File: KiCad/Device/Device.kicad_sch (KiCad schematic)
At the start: 29 parts, among them IC1 ATTINY167-XUR, J1 Mikrofon, J2 Lysføler, J3 Optisk sensor, J4 Fugtføler, J5 VCC, J6 ESP8266(wifi), J7 Conn_02x06_Counter_Clockwise, SW1 SW_MEC_5E, SW3 SW_MEC_5E, SW4 SW_DIP_x02, Y1 Crystal

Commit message: save
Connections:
- net +5V: now also J7.11 (Pin_11); no longer J7.12 (Pin_12)
- net UPWR: now also J7.12 (Pin_12); no longer J7.11 (Pin_11)
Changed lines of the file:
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@@
     (stroke (width 0) (type default) (color 0 0 0 0))
   )
-  (wire (pts (xy 243.84 119.38) (xy 229.87 119.38))
+  (wire (pts (xy 243.84 119.38) (xy 234.95 119.38))
     (stroke (width 0) (type default) (color 0 0 0 0))
   )
@@
     (stroke (width 0) (type default) (color 0 0 0 0))
   )
+  (wire (pts (xy 256.54 119.38) (xy 267.335 119.38))
+    (stroke (width 0) (type default) (color 0 0 0 0))
+  )
   (wire (pts (xy 77.47 177.8) (xy 81.28 177.8))
     (stroke (width 0) (type default) (color 0 0 0 0))
@@
     (stroke (width 0) (type default) (color 0 0 0 0))
   )
-  (wire (pts (xy 243.84 116.84) (xy 224.155 116.84))
+  (wire (pts (xy 243.84 116.84) (xy 229.235 116.84))
     (stroke (width 0) (type default) (color 0 0 0 0))
   )
@@
     )
   )
-  (global_label "UPWR" (shape input) (at 256.54 119.38 0) (fields_autoplaced)
-    (effects (font (size 1.27 1.27)) (justify left))
-    (property "Intersheet References" "${INTERSHEET_REFS}" (id 0) (at 264.275 119.4594 0)
+  (global_label "UPWR" (shape input) (at 256.54 116.84 0) (fields_autoplaced)
+    (effects (font (size 1.27 1.27)) (justify left))
+    (property "Intersheet References" "${INTERSHEET_REFS}" (id 0) (at 264.275 116.9194 0)
       (effects (font (size 1.27 1.27)) (justify left) hide)
     )
@@
     (pin "1")
   )
-  (symbol (lib_id "power:GND") (at 229.87 119.38 0) (mirror y) (unit 1)
-    (in_bom yes) (on_board yes)
-    (property "Reference" "#PWR0118" (id 0) (at 229.87 125.73 0)
-      (effects (font (size 1.27 1.27)) hide)
-    )
-    (property "Value" "GND" (id 1) (at 231.775 123.19 0)
-      (effects (font (size 1.27 1.27)) (justify left))
-    )
-    (property "Footprint" "" (id 2) (at 229.87 119.38 0)
-      (effects (font (size 1.27 1.27)) hide)
-    )
-    (property "Datasheet" "" (id 3) (at 229.87 119.38 0)
+  (symbol (lib_id "power:GND") (at 234.95 119.38 0) (mirror y) (unit 1)
+    (in_bom yes) (on_board yes)
+    (property "Reference" "#PWR0118" (id 0) (at 234.95 125.73 0)
+      (effects (font (size 1.27 1.27)) hide)
+    )
+    (property "Value" "GND" (id 1) (at 236.855 123.19 0)
+      (effects (font (size 1.27 1.27)) (justify left))
+    )
+    (property "Footprint" "" (id 2) (at 234.95 119.38 0)
+      (effects (font (size 1.27 1.27)) hide)
+    )
+    (property "Datasheet" "" (id 3) (at 234.95 119.38 0)
       (effects (font (size 1.27 1.27)) hide)
     )
@@
     (pin "2")
   )
-  (symbol (lib_id "power:+5V") (at 256.54 116.84 0) (mirror y) (unit 1)
-    (in_bom yes) (on_board yes)
-    (property "Reference" "#PWR0102" (id 0) (at 256.54 120.65 0)
-      (effects (font (size 1.27 1.27)) hide)
-    )
-    (property "Value" "+5V" (id 1) (at 259.715 115.57 0))
-    (property "Footprint" "" (id 2) (at 256.54 116.84 0)
-      (effects (font (size 1.27 1.27)) hide)
-    )
-    (property "Datasheet" "" (id 3) (at 256.54 116.84 0)
+  (symbol (lib_id "power:+5V") (at 267.335 119.38 0) (mirror y) (unit 1)
+    (in_bom yes) (on_board yes)
+    (property "Reference" "#PWR0102" (id 0) (at 267.335 123.19 0)
+      (effects (font (size 1.27 1.27)) hide)
+    )
+    (property "Value" "+5V" (id 1) (at 270.51 118.11 0))
+    (property "Footprint" "" (id 2) (at 267.335 119.38 0)
+      (effects (font (size 1.27 1.27)) hide)
+    )
+    (property "Datasheet" "" (id 3) (at 267.335 119.38 0)
       (effects (font (size 1.27 1.27)) hide)
     )
@@
     (pin "1")
   )
-  (symbol (lib_id "power:GND") (at 224.155 116.84 0) (mirror y) (unit 1)
-    (in_bom yes) (on_board yes)
-    (property "Reference" "#PWR0101" (id 0) (at 224.155 123.19 0)
-      (effects (font (size 1.27 1.27)) hide)
-    )
-    (property "Value" "GND" (id 1) (at 226.06 120.65 0)
-      (effects (font (size 1.27 1.27)) (justify left))
-    )
-    (property "Footprint" "" (id 2) (at 224.155 116.84 0)
-      (effects (font (size 1.27 1.27)) hide)
-    )
-    (property "Datasheet" "" (id 3) (at 224.155 116.84 0)
-      (effects (font (size 1.27 1.27)) hide)
-    )
+  (symbol (lib_id "power:GND") (at 229.235 116.84 0) (mirror y) (unit 1)
+    (in_bom yes) (on_board yes)
+    (property "Reference" "#PWR0101" (id 0) (at 229.235 123.19 0)
+      (effects (font (size 1.27 1.27)) hide)
+    )
+    (property "Value" "GND" (id 1) (at 231.14 120.65 0)
+      (effects (font (size 1.27 1.27)) (justify left))
+    )
+    (property "Footprint" "" (id 2) (at 229.235 116.84 0)
+      (effects (font (size 1.27 1.27)) hide)
+    )
+    (property "Datasheet" "" (id 3) (at 229.235 116.84 0)
+      (effects (font (size 1.27 1.27)) hide)
+    )

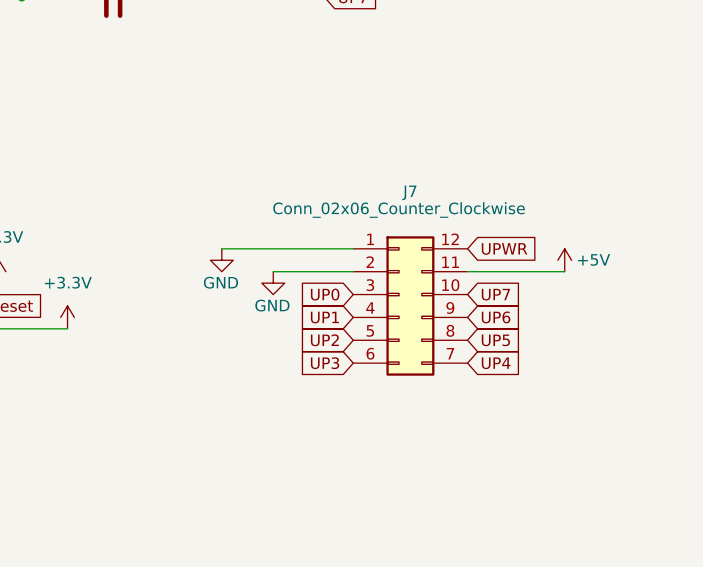
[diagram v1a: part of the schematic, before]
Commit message: Ny_connecter
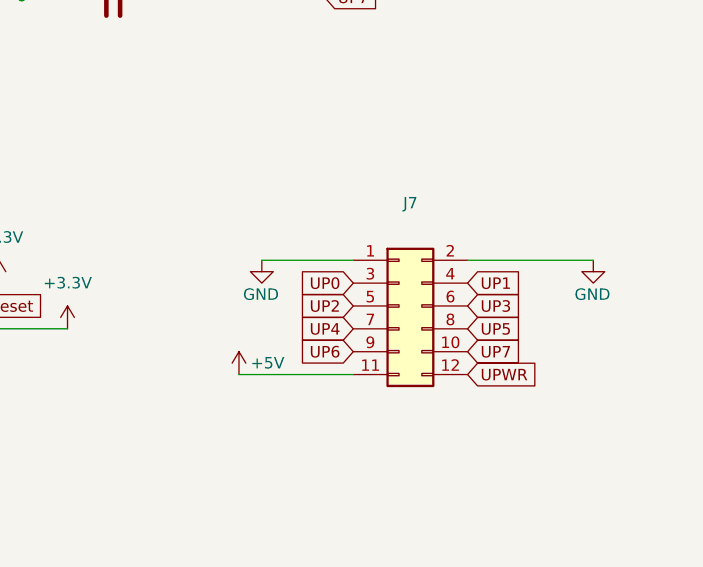
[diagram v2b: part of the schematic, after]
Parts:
- removed J7: Conn_02x06_Counter_Clockwise, Connector_PinHeader_2.54mm:PinHeader_2x06_P2.54mm_Horizontal, symbol Connector_Generic:Conn_02x06_Counter_Clockwise
- added J7: (no value), symbol Connector_Generic:Conn_02x06_Odd_Even
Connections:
- net +5V: now also J7.11 (Pin_11)
- net DHT11: now also J7.3 (Pin_3)
- net GND: now also J7.1 (Pin_1), J7.2 (Pin_2)
- net OPTISK: now also J7.6 (Pin_6)
- net PHOTRAN: now also J7.9 (Pin_9)
- net UP1: now also J7.4 (Pin_4)
- net UP2: now also J7.5 (Pin_5)
- net UP4: now also J7.7 (Pin_7)
- net UP5: now also J7.8 (Pin_8)
- net UP7: now also J7.10 (Pin_10)
- net UPWR: now also J7.12 (Pin_12)

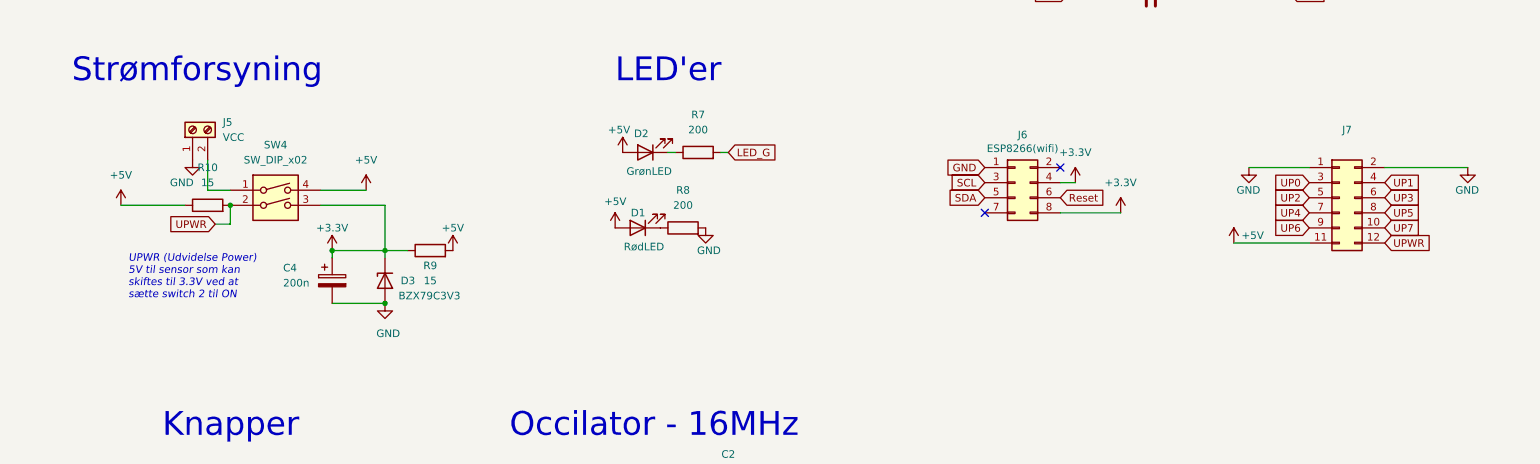
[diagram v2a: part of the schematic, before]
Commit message: Opdatering af device kicad
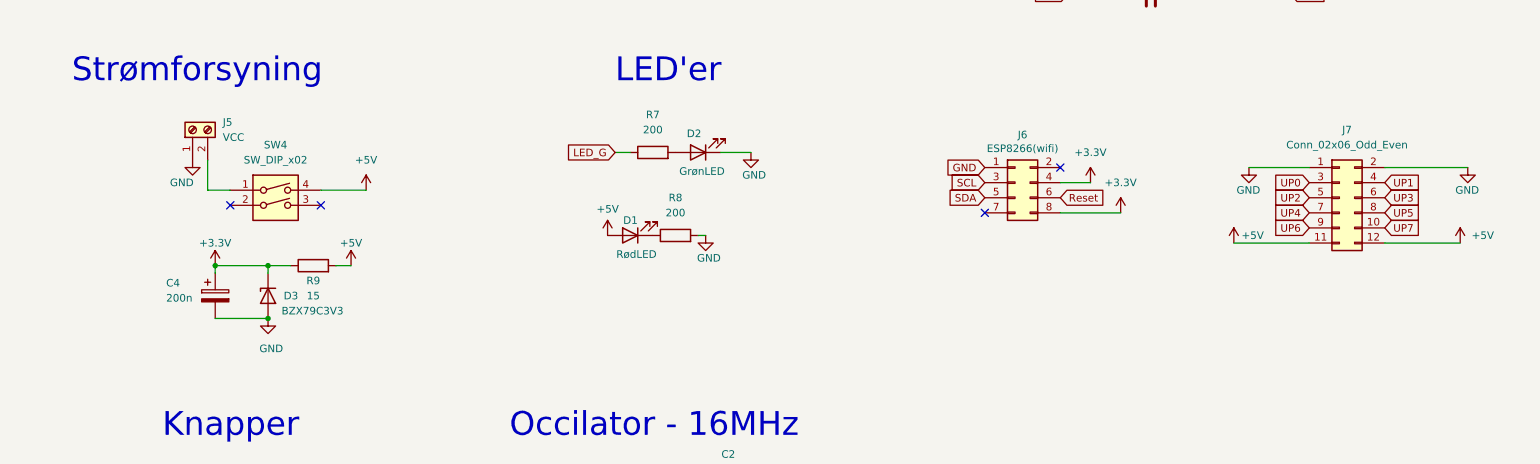
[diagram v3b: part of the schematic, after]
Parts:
- removed R10: 15, Resistor_THT:R_Axial_DIN0309_L9.0mm_D3.2mm_P12.70mm_Horizontal, symbol Device:R
- J7: value (none) -> Conn_02x06_Odd_Even; footprint (none) -> Connector_PinHeader_2.54mm:PinHeader_2x06_P2.54mm_Vertical
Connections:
- net +3V3: no longer SW4.3
- net +5V: now also J7.12 (Pin_12); no longer D2.2 (A)
- net GND: now also D2.1 (K)
- net LED_G: now also R7.1; no longer R7.2
- net UPWR: no longer names the net of SW4.2
- net UPWR: no longer J7.12 (Pin_12)
- new net: D2.2 (A), R7.2
- no-connect marks 3 -> 5
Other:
- note removed: "UPWR (Udvidelse Power) 5V til sensor som kan skiftes til 3.3V ved at sætte switch 2 til ON"
- moved on the sheet: C4, D1, D2, D3, R7, R8, R9

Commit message: Opdateret pcb
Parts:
- added R11: (no value), symbol Device:R
- added R12: 4.7k, symbol Device:R
- renumbered R9 to R10
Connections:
- net +3V3: now also R11.2, R12.2
- net SCL: now also R12.1
- net SDA: now also R11.1
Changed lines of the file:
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@@
   (junction (at 77.47 177.8) (diameter 0) (color 0 0 0 0)
   )
+  (junction (at 175.26 120.65) (diameter 0) (color 0 0 0 0)
+  )
   (junction (at 59.69 134.62) (diameter 0) (color 0 0 0 0)
   )
@@
   )
   (junction (at 67.31 177.8) (diameter 0) (color 0 0 0 0)
+  )
+  (junction (at 175.26 138.43) (diameter 0) (color 0 0 0 0)
   )
   (junction (at 207.01 88.9) (diameter 0) (color 0 0 0 0)
@@
     (stroke (width 0) (type default) (color 0 0 0 0))
   )
+  (wire (pts (xy 175.26 135.89) (xy 175.26 138.43))
+    (stroke (width 0) (type default) (color 0 0 0 0))
+  )
   (wire (pts (xy 220.98 88.9) (xy 240.665 88.9))
     (stroke (width 0) (type default) (color 0 0 0 0))
@@
     (stroke (width 0) (type default) (color 0 0 0 0))
   )
+  (wire (pts (xy 175.26 138.43) (xy 185.42 138.43))
+    (stroke (width 0) (type default) (color 0 0 0 0))
+  )
   (wire (pts (xy 27.94 182.88) (xy 27.94 185.42))
     (stroke (width 0) (type default) (color 0 0 0 0))
@@
     (stroke (width 0) (type default) (color 0 0 0 0))
   )
+  (wire (pts (xy 189.23 123.19) (xy 185.42 123.19))
+    (stroke (width 0) (type default) (color 0 0 0 0))
+  )
+  (wire (pts (xy 170.18 138.43) (xy 175.26 138.43))
+    (stroke (width 0) (type default) (color 0 0 0 0))
+  )
   (wire (pts (xy 269.24 130.81) (xy 256.54 130.81))
     (stroke (width 0) (type default) (color 0 0 0 0))
   )
+  (wire (pts (xy 185.42 123.19) (xy 185.42 138.43))
+    (stroke (width 0) (type default) (color 0 0 0 0))
+  )
   (wire (pts (xy 153.67 173.99) (xy 149.86 173.99))
     (stroke (width 0) (type default) (color 0 0 0 0))
@@
     (stroke (width 0) (type default) (color 0 0 0 0))
   )
+  (wire (pts (xy 170.18 120.65) (xy 175.26 120.65))
+    (stroke (width 0) (type default) (color 0 0 0 0))
+  )
   (wire (pts (xy 256.54 118.11) (xy 270.51 118.11))
     (stroke (width 0) (type default) (color 0 0 0 0))
@@
     (stroke (width 0) (type default) (color 0 0 0 0))
   )
+  (wire (pts (xy 175.26 120.65) (xy 189.23 120.65))
+    (stroke (width 0) (type default) (color 0 0 0 0))
+  )
   (wire (pts (xy 77.47 177.8) (xy 81.28 177.8))
     (stroke (width 0) (type default) (color 0 0 0 0))
@@
   )
   (wire (pts (xy 254 36.83) (xy 257.81 36.83))
+    (stroke (width 0) (type default) (color 0 0 0 0))
+  )
+  (wire (pts (xy 175.26 118.11) (xy 175.26 120.65))
     (stroke (width 0) (type default) (color 0 0 0 0))
   )
@@
     )
   )
+  (global_label "SCL" (shape input) (at 170.18 120.65 180) (fields_autoplaced)
+    (effects (font (size 1.27 1.27)) (justify right))
+    (property "Intersheet References" "${INTERSHEET_REFS}" (id 0) (at 164.2593 120.5706 0)
+      (effects (font (size 1.27 1.27)) (justify right) hide)
+    )
+  )
   (global_label "UP6" (shape input) (at 240.665 86.36 0) (fields_autoplaced)
     (effects (font (size 1.27 1.27)) (justify left))
@@
     )
   )
-  (global_label "SCL" (shape input) (at 189.23 120.65 180) (fields_autoplaced)
-    (effects (font (size 1.27 1.27)) (justify right))
-    (property "Intersheet References" "${INTERSHEET_REFS}" (id 0) (at 183.3093 120.5706 0)
-      (effects (font (size 1.27 1.27)) (justify right) hide)
-    )
-  )
   (global_label "UP2" (shape input) (at 240.665 74.93 0) (fields_autoplaced)
     (effects (font (size 1.27 1.27)) (justify left))
@@
     )
   )
-  (global_label "SDA" (shape input) (at 189.23 123.19 180) (fields_autoplaced)
-    (effects (font (size 1.27 1.27)) (justify right))
-    (property "Intersheet References" "${INTERSHEET_REFS}" (id 0) (at 183.2488 123.1106 0)
+  (global_label "SDA" (shape input) (at 170.18 138.43 180) (fields_autoplaced)
+    (effects (font (size 1.27 1.27)) (justify right))
+    (property "Intersheet References" "${INTERSHEET_REFS}" (id 0) (at 164.1988 138.3506 0)
       (effects (font (size 1.27 1.27)) (justify right) hide)
     )
@@
     (pin "1")
     (pin "2")
+    (pin "2")
+  )
+  (symbol (lib_id "Device:R") (at 175.26 114.3 180) (unit 1)
+    (in_bom yes) (on_board yes) (fields_autoplaced)
+    (property "Reference" "R12" (id 0) (at 177.8 113.0299 0)
+      (effects (font (size 1.27 1.27)) (justify right))
+    )
+    (property "Value" "4.7k" (id 1) (at 177.8 115.5699 0)
+      (effects (font (size 1.27 1.27)) (justify right))
+    )
+    (property "Footprint" "" (id 2) (at 177.038 114.3 90)
+      (effects (font (size 1.27 1.27)) hide)
+    )
+    (property "Datasheet" "~" (id 3) (at 175.26 114.3 0)
+      (effects (font (size 1.27 1.27)) hide)
+    )
+    (pin "1")
     (pin "2")
   )
@@
     (pin "1")
   )
+  (symbol (lib_id "power:+3.3V") (at 175.26 128.27 0) (mirror y) (unit 1)
+    (in_bom yes) (on_board yes)
+    (property "Reference" "#PWR0131" (id 0) (at 175.26 132.08 0)
+      (effects (font (size 1.27 1.27)) hide)
+    )
+    (property "Value" "+3.3V" (id 1) (at 175.26 124.46 0))
+    (property "Footprint" "" (id 2) (at 175.26 128.27 0)
+      (effects (font (size 1.27 1.27)) hide)
+    )
+    (property "Datasheet" "" (id 3) (at 175.26 128.27 0)
+      (effects (font (size 1.27 1.27)) hide)
+    )
+    (pin "1")
+  )
   (symbol (lib_id "Device:R") (at 76.2 134.62 90) (unit 1)
     (in_bom yes) (on_board yes)
-    (property "Reference" "R9" (id 0) (at 76.2 137.16 90))
+    (property "Reference" "R10" (id 0) (at 76.2 137.16 90))
     (property "Value" "15" (id 1) (at 76.2 139.7 90))
     (property "Footprint" "Resistor_THT:R_Axial_DIN0309_L9.0mm_D3.2mm_P12.70mm_Horizontal" (id 2) (at 76.2 136.398 90)
@@
     )
     (pin "1")
+  )
+  (symbol (lib_id "Device:R") (at 175.26 132.08 180) (unit 1)
+    (in_bom yes) (on_board yes) (fields_autoplaced)
+    (property "Reference" "R11" (id 0) (at 177.8 130.8099 0)
+      (effects (font (size 1.27 1.27)) (justify right))
+    )
+    (property "Value" "" (id 1) (at 177.8 133.3499 0)
+      (effects (font (size 1.27 1.27)) (justify right))
+    )
+    (property "Footprint" "" (id 2) (at 177.038 132.08 90)
+      (effects (font (size 1.27 1.27)) hide)
+    )
+    (property "Datasheet" "~" (id 3) (at 175.26 132.08 0)
+      (effects (font (size 1.27 1.27)) hide)
+    )
+    (pin "1")
+    (pin "2")
   )
   (symbol (lib_id "power:GND") (at 81.28 185.42 0) (unit 1)
@@
     (pin "1")
   )
+  (symbol (lib_id "power:+3.3V") (at 175.26 110.49 0) (mirror y) (unit 1)
+    (in_bom yes) (on_board yes)
+    (property "Reference" "#PWR0130" (id 0) (at 175.26 114.3 0)
+      (effects (font (size 1.27 1.27)) hide)
+    )
+    (property "Value" "+3.3V" (id 1) (at 175.26 106.68 0))
+    (property "Footprint" "" (id 2) (at 175.26 110.49 0)
+      (effects (font (size 1.27 1.27)) hide)
+    )
+    (property "Datasheet" "" (id 3) (at 175.26 110.49 0)
+      (effects (font (size 1.27 1.27)) hide)
+    )
+    (pin "1")
+  )
   (symbol (lib_id "power:+3.3V") (at 59.69 134.62 0) (mirror y) (unit 1)
     (in_bom yes) (on_board yes)
@@
       (reference "#PWR0129") (unit 1) (value "+5V") (footprint "")
     )
+    (path "/c1a2b104-b142-45b8-b862-a8429affbf64"
+      (reference "#PWR0130") (unit 1) (value "+3.3V") (footprint "")
+    )
+    (path "/20b00bfc-ccbf-4118-abcf-2be697c972b1"
+      (reference "#PWR0131") (unit 1) (value "+3.3V") (footprint "")
+    )
     (path "/c3859b88-ee1c-4daa-9fe4-63386a16086c"
       (reference "C1") (unit 1) (value "1uF") (footprint "Capacitor_THT:C_Disc_D5.0mm_W2.5mm_P5.00mm")
@@
     )
     (path "/22a624b4-92d7-43d1-8e9e-a4d7a24dcfef"
-      (reference "R9") (unit 1) (value "15") (footprint "Resistor_THT:R_Axial_DIN0309_L9.0mm_D3.2mm_P12.70mm_Horizontal")
+      (reference "R10") (unit 1) (value "15") (footprint "Resistor_THT:R_Axial_DIN0309_L9.0mm_D3.2mm_P12.70mm_Horizontal")
+    )
+    (path "/47137ae1-6e37-474c-a18c-7434b2cf6e64"
+      (reference "R11") (unit 1) (value "4.7k") (footprint "Resistor_THT:R_Axial_DIN0309_L9.0mm_D3.2mm_P12.70mm_Horizontal")
+    )
+    (path "/166cc9f8-2195-46c9-879b-2772f3aa013f"
+      (reference "R12") (unit 1) (value "4.7k") (footprint "Resistor_THT:R_Axial_DIN0309_L9.0mm_D3.2mm_P12.70mm_Horizontal")
     )
     (path "/a54f7712-51f6-4eb0-80d4-0e09613d050b"

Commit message: Update Device.kicad_sch
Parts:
- R1: value 10k -> (none)
- R11: value (none) -> 4.7k; footprint (none) -> Resistor_THT:R_Axial_DIN0309_L9.0mm_D3.2mm_P12.70mm_Horizontal
- R12: footprint (none) -> Resistor_THT:R_Axial_DIN0309_L9.0mm_D3.2mm_P12.70mm_Horizontal
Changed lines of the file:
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@@
       (effects (font (size 1.27 1.27)) (justify right))
     )
-    (property "Footprint" "" (id 2) (at 177.038 114.3 90)
+    (property "Footprint" "Resistor_THT:R_Axial_DIN0309_L9.0mm_D3.2mm_P12.70mm_Horizontal" (id 2) (at 177.038 114.3 90)
       (effects (font (size 1.27 1.27)) hide)
     )
@@
       (effects (font (size 1.27 1.27)) (justify right))
     )
-    (property "Value" "" (id 1) (at 177.8 133.3499 0)
-      (effects (font (size 1.27 1.27)) (justify right))
-    )
-    (property "Footprint" "" (id 2) (at 177.038 132.08 90)
+    (property "Value" "4.7k" (id 1) (at 177.8 133.3499 0)
+      (effects (font (size 1.27 1.27)) (justify right))
+    )
+    (property "Footprint" "Resistor_THT:R_Axial_DIN0309_L9.0mm_D3.2mm_P12.70mm_Horizontal" (id 2) (at 177.038 132.08 90)
       (effects (font (size 1.27 1.27)) hide)
     )
@@
       (effects (font (size 1.27 1.27)) (justify left))
     )
-    (property "Value" "10k" (id 1) (at 99.06 64.7699 0)
+    (property "Value" "" (id 1) (at 99.06 64.7699 0)
       (effects (font (size 1.27 1.27)) (justify left))
     )
@@
     )
     (path "/de92152a-3f95-470e-8a68-519c1291418b"
-      (reference "R1") (unit 1) (value "10k") (footprint "Resistor_THT:R_Axial_DIN0309_L9.0mm_D3.2mm_P12.70mm_Horizontal")
+      (reference "R1") (unit 1) (value "1k") (footprint "Resistor_THT:R_Axial_DIN0309_L9.0mm_D3.2mm_P12.70mm_Horizontal")
     )
     (path "/d8200a86-aa75-47a3-ad2a-7f4c9c999a6f"
